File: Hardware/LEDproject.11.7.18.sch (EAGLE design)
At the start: 14 parts, among them IC1 ATMEGA328-PU, Y1 16MHz

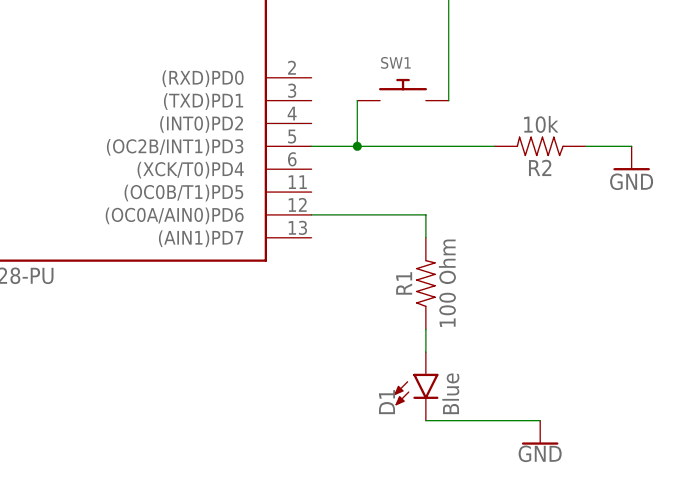
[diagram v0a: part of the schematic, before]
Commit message: updated breadboard and circuit to match schematics
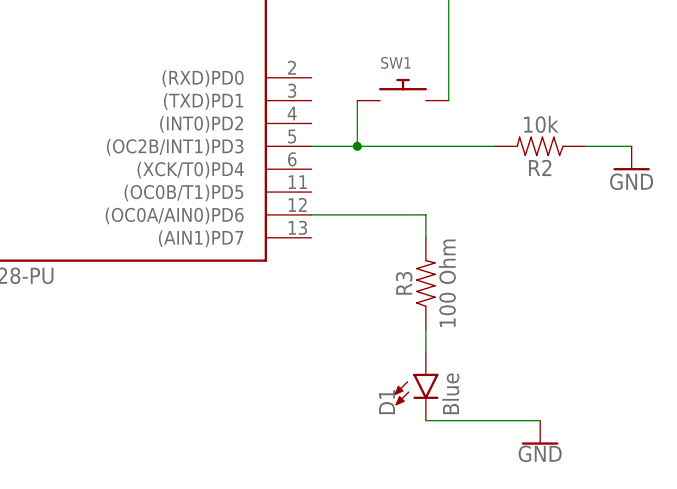
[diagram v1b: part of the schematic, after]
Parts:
- removed R1: 100 Ohm, SparkFun-Resistors:150OHM-0603-1/10W-1%
- added R3: 100 Ohm, SparkFun-Resistors:10KOHM-HORIZ-1/4W-1%
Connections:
- net N$7: now also R3.2; no longer R1.2
- net N$8: now also R3.1; no longer R1.1
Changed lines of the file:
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@@
 </variantdefs>
 <classes>
-<class number="0" name="default" width="0" drill="0">
+<class number="0" name="default" width="0.3048" drill="0.508">
+<clearance class="0" value="0.254"/>
 </class>
 </classes>
@@
 </part>
 <part name="GND6" library="SparkFun-PowerSymbols" library_urn="urn:adsk.eagle:library:530" deviceset="GND" device=""/>
-<part name="R1" library="SparkFun-Resistors" library_urn="urn:adsk.eagle:library:532" deviceset="150OHM" device="-0603-1/10W-1%" package3d_urn="urn:adsk.eagle:package:39650/1" value="100 Ohm"/>
 <part name="GND7" library="SparkFun-PowerSymbols" library_urn="urn:adsk.eagle:library:530" deviceset="GND" device=""/>
 <part name="SUPPLY1" library="supply2" library_urn="urn:adsk.eagle:library:372" deviceset="+5V" device=""/>
@@
 <part name="C4" library="adafruit" library_urn="urn:adsk.eagle:library:420" deviceset="C-US" device="025-030X050" package3d_urn="urn:adsk.eagle:package:6240322/1" value=".1uF"/>
 <part name="C5" library="adafruit" library_urn="urn:adsk.eagle:library:420" deviceset="C-US" device="025-030X050" package3d_urn="urn:adsk.eagle:package:6240322/1" value=".1 uF"/>
+<part name="R3" library="SparkFun-Resistors" library_urn="urn:adsk.eagle:library:532" deviceset="10KOHM" device="-HORIZ-1/4W-1%" package3d_urn="urn:adsk.eagle:package:39658/1" value="100 Ohm"/>
 </parts>
 <sheets>
@@
 <attribute name="VALUE" x="58.42" y="73.406" size="1.778" layer="96" align="top-center"/>
 </instance>
-<instance part="R1" gate="G$1" x="104.14" y="2.54" rot="R90">
-<attribute name="NAME" x="102.616" y="2.54" size="1.778" layer="95" font="vector" rot="R90" align="bottom-center"/>
-<attribute name="VALUE" x="105.664" y="2.54" size="1.778" layer="96" font="vector" rot="R90" align="top-center"/>
-</instance>
 <instance part="GND7" gate="1" x="116.84" y="-15.24">
 <attribute name="VALUE" x="116.84" y="-15.494" size="1.778" layer="96" align="top-center"/>
@@
 <attribute name="NAME" x="45.085" y="77.216" size="1.778" layer="95" rot="R90"/>
 <attribute name="VALUE" x="49.911" y="77.216" size="1.778" layer="96" rot="R90"/>
+</instance>
+<instance part="R3" gate="G$1" x="104.14" y="2.54" rot="R90">
+<attribute name="NAME" x="102.616" y="2.54" size="1.778" layer="95" font="vector" rot="R90" align="bottom-center"/>
+<attribute name="VALUE" x="105.664" y="2.54" size="1.778" layer="96" font="vector" rot="R90" align="top-center"/>
 </instance>
 </instances>
@@
 <segment>
 <pinref part="IC1" gate="IC" pin="(OC0A/AIN0)PD6"/>
-<pinref part="R1" gate="G$1" pin="2"/>
 <wire x1="91.44" y1="10.16" x2="104.14" y2="10.16" width="0.1524" layer="91"/>
 <wire x1="104.14" y1="10.16" x2="104.14" y2="7.62" width="0.1524" layer="91"/>
+<pinref part="R3" gate="G$1" pin="2"/>
 </segment>
 </net>
 <net name="N$8" class="0">
 <segment>
-<pinref part="R1" gate="G$1" pin="1"/>
 <pinref part="D1" gate="G$1" pin="A"/>
 <wire x1="104.14" y1="-2.54" x2="104.14" y2="-5.08" width="0.1524" layer="91"/>
-</segment>
-</net>
+<pinref part="R3" gate="G$1" pin="1"/>
+</segment>
+</net>
